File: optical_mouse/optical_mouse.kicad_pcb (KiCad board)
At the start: 2 copper layers, 44.5 x 45.7 mm, 18 parts, among them Q1 CSTLS_G, U1 ARDUINO_MINI

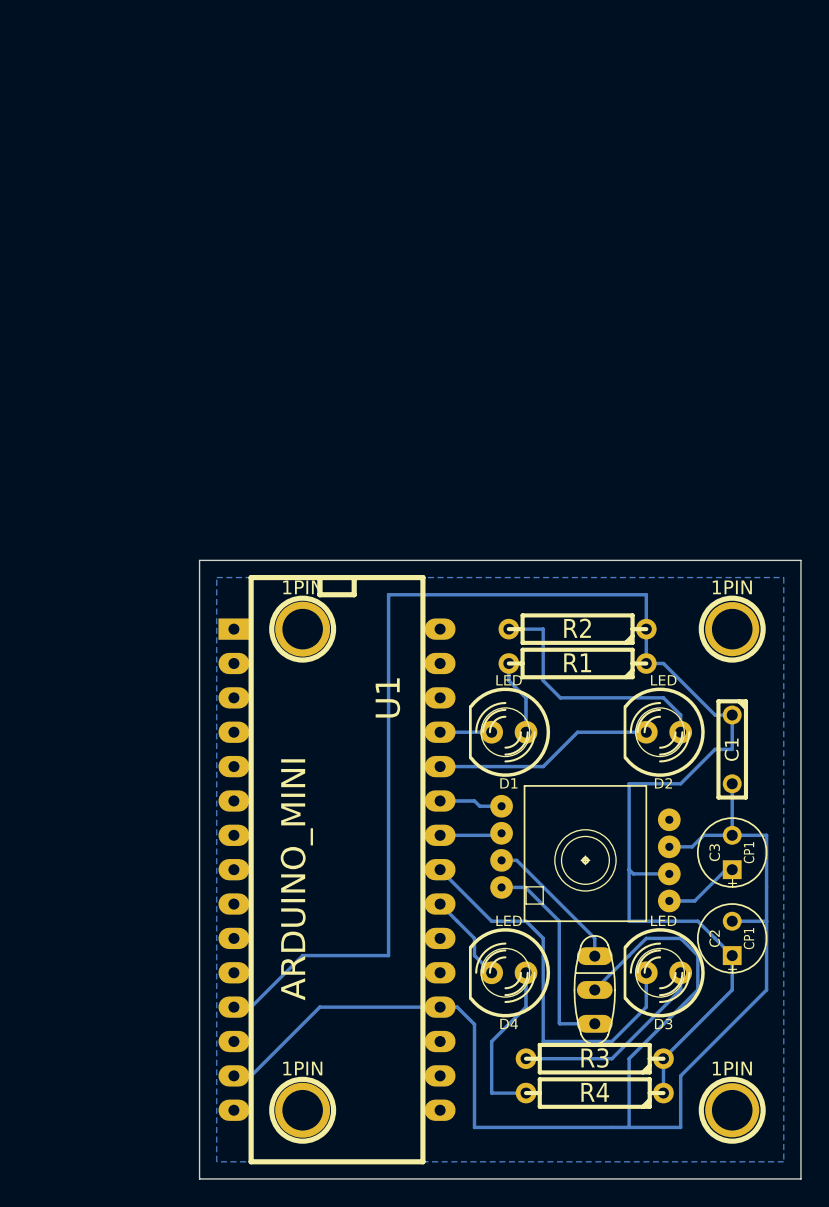
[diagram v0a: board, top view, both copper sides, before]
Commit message: re-layed out with correct mouse part
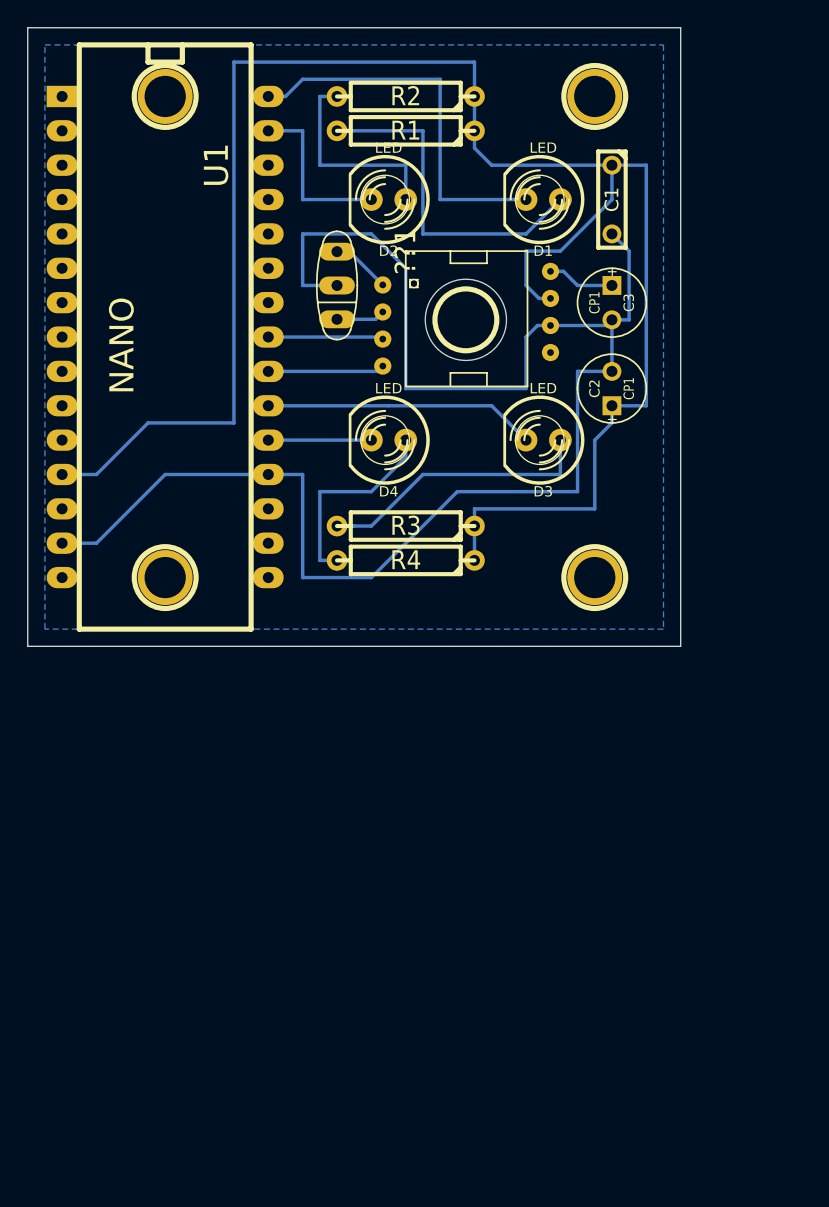
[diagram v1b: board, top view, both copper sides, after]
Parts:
- removed 1PIN (x4): P***, 1pin
- added ?: , 1pin, F.Cu at (154.9, 110.5)
- added ?: , 1pin, F.Cu at (186.7, 110.5)
- added ?: , 1pin, F.Cu at (186.7, 146.1)
- added ?: , 1pin, F.Cu at (154.9, 146.1)
- added ?: , 1pin, F.Cu at (177.2, 127.0)
- ??1: value ANDS-2610 -> (none); footprint adns-2610-DIP-8 -> adns-2610-DIP-8_(GORA)
- U1: value ARDUINO_MINI -> NANO
- moved Q1 55.4 mm to (167.6, 124.5), turned to 90 degrees
- moved ??1 52.6 mm to (172.7, 121.9), turned to 270 degrees
- moved D2 44.3 mm to (171.4, 118.1)
- moved R3 41.8 mm to (172.7, 142.2)
- moved R4 41.8 mm to (172.7, 144.8)
- moved C1 41.6 mm to (188.0, 118.1)
- moved C3 41.6 mm to (188.0, 125.7), turned to 270 degrees
- moved C2 41.6 mm to (188.0, 132.1)
- moved R2 41.4 mm to (172.7, 110.5)
- moved R1 41.4 mm to (172.7, 113.0)
- moved U1 41.4 mm to (154.9, 129.5)
- moved D3 40.4 mm to (182.9, 135.9)
- moved D4 40.4 mm to (171.4, 135.9)
- moved D1 39.5 mm to (182.9, 118.1)
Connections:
- ??1 pad 3: N-0000028 -> N-0000024
- ??1 pad 4: N-0000029 -> N-0000022
- D1 pad 2: N-000004 -> N-0000019
- D2 pad 2: N-000002 -> N-000006
- D3 pad 2: N-0000027 -> N-0000011
- D4 pad 2: N-0000025 -> N-0000018
- U1 pad 20: (no net) -> N-0000018
- U1 pad 21: (no net) -> N-0000011
- U1 pad 22: N-0000025 -> N-0000022
- U1 pad 23: N-0000027 -> N-0000024
- U1 pad 24: N-0000028 -> (no net)
- U1 pad 25: N-0000029 -> (no net)
- U1 pad 26: N-000002 -> (no net)
- U1 pad 27: N-000004 -> (no net)
- U1 pad 29: (no net) -> N-000006
- U1 pad 30: (no net) -> N-0000019
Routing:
- net N-0000027: track 28.6 -> 0.00 mm
- net N-0000019: track 0.00 -> 28.5 mm
- net N-0000011: track 0.00 -> 20.1 mm
- net N-000007: track 5.61 -> 25.2 mm
- net +5V: track 117.1 -> 134.7 mm
- net N-000002: track 16.3 -> 0.00 mm
- net N-000006: track 0.00 -> 12.7 mm
- net GND: track 105.9 -> 117.3 mm
- net N-0000032: track 15.5 -> 4.40 mm
- net N-0000022: track 0.00 -> 8.62 mm
- net N-0000024: track 0.00 -> 8.52 mm
- net N-0000018: track 0.00 -> 7.62 mm
- net N-0000031: track 10.6 -> 3.60 mm
- net N-0000025: track 6.66 -> 0.00 mm
- net N-000009: track 14.8 -> 20.6 mm
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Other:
- board size 44.5 x 45.7 mm -> 48.3 x 45.7 mm
- board text removed: "OptiMouseCam v 1.0 (C) Dave Berkeley 2015"

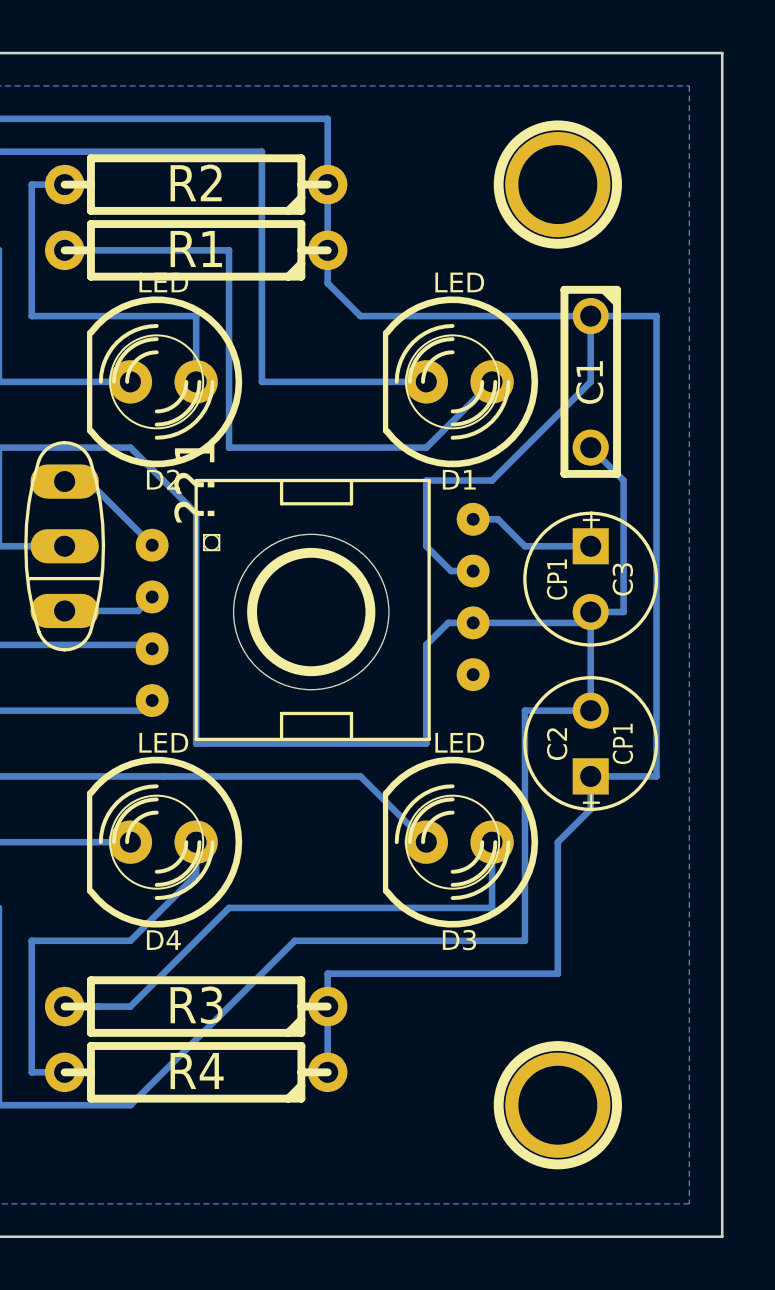
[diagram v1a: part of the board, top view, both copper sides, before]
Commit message: ensure camera hole is drilled in seedstudio
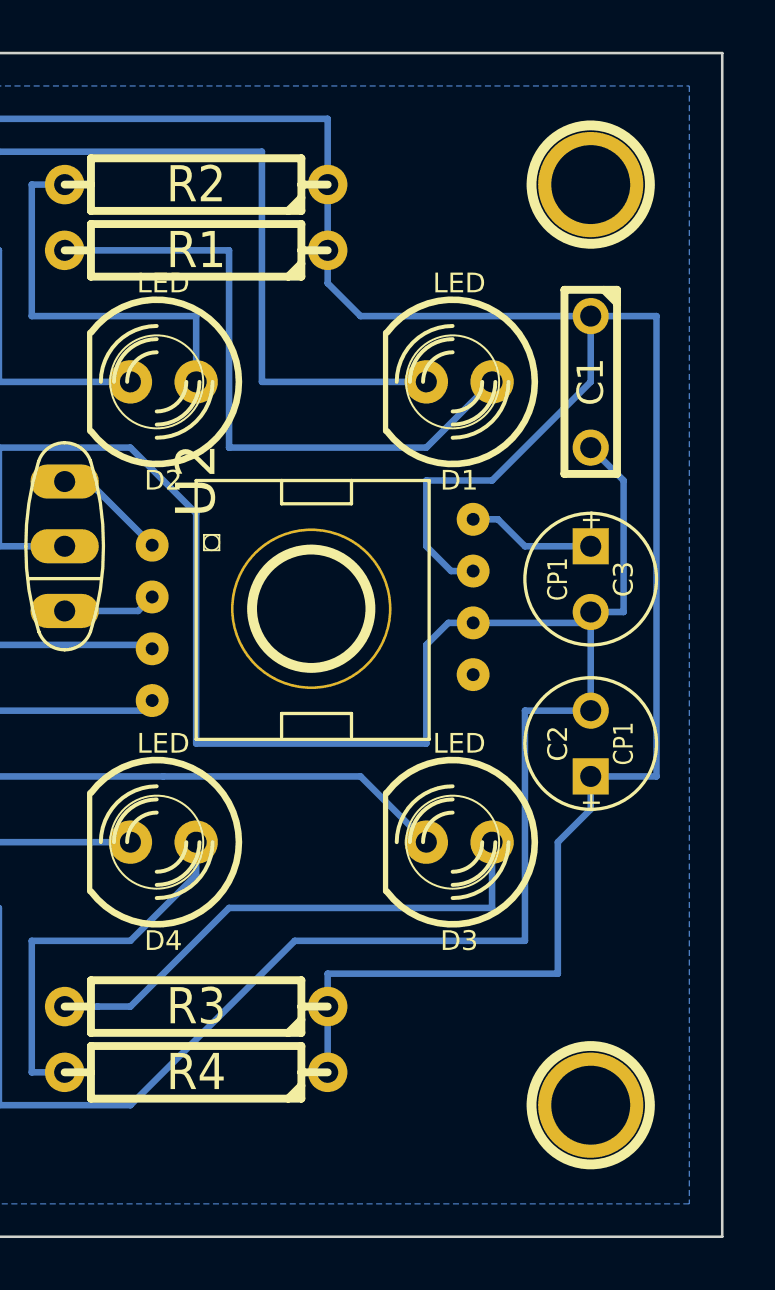
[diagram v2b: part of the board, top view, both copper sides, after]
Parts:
- moved ? 48.5 mm to (188.0, 146.1)
- moved ? 35.6 mm to (154.9, 110.5)
- moved ? 31.8 mm to (154.9, 146.1)
- moved ? 1.27 mm to (188.0, 110.5)
- moved ? 0.13 mm to (177.2, 126.9)
- renumbered ??1 to U2
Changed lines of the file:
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@@
     (mod_text_size 1 1)
     (mod_text_width 0.15)
-    (pad_size 6 6)
+    (pad_size 6.2 6.2)
     (pad_drill 6)
     (pad_to_mask_clearance 0)
@@
     (at 172.72 121.92 270)
     (attr virtual)
-    (fp_text reference ??1 (at 0 0 270) (layer F.SilkS)
+    (fp_text reference U2 (at 0 0 270) (layer F.SilkS)
       (effects (font (size 1.524 1.524) (thickness 0.15)))
     )
@@
   )
   (module 1pin (layer F.Cu)
-    (at 154.94 110.49)
+    (at 187.96 146.05)
     (descr "module 1 pin (ou trou mecanique de percage)")
     (tags DEV)
@@
     )
     (fp_circle (center 0 0) (end 0 -2.286) (layer F.SilkS) (width 0.381))
-    (pad "" np_thru_hole circle (at 0 0) (size 4.064 4.064) (drill 3.048)
+    (pad "" thru_hole circle (at 0 0) (size 4.064 4.064) (drill 3.048)
       (layers *.Cu *.Mask F.SilkS)
     )
   )
   (module 1pin (layer F.Cu)
-    (at 186.69 110.49)
+    (at 187.96 110.49)
     (descr "module 1 pin (ou trou mecanique de percage)")
     (tags DEV)
@@
     )
     (fp_circle (center 0 0) (end 0 -2.286) (layer F.SilkS) (width 0.381))
-    (pad "" np_thru_hole circle (at 0 0) (size 4.064 4.064) (drill 3.048)
-      (layers *.Cu *.Mask F.SilkS)
-    )
-  )
-  (module 1pin (layer F.Cu)
-    (at 186.69 146.05)
-    (descr "module 1 pin (ou trou mecanique de percage)")
-    (tags DEV)
-    (path 1pin)
-    (fp_text reference "" (at 0 -3.048) (layer F.SilkS)
-      (effects (font (size 1.016 1.016) (thickness 0.254)))
-    )
-    (fp_text value "" (at 0 2.794) (layer F.SilkS) hide
-      (effects (font (size 1.016 1.016) (thickness 0.254)))
-    )
-    (fp_circle (center 0 0) (end 0 -2.286) (layer F.SilkS) (width 0.381))
-    (pad "" np_thru_hole circle (at 0 0) (size 4.064 4.064) (drill 3.048)
+    (pad "" thru_hole circle (at 0 0) (size 4.064 4.064) (drill 3.048)
       (layers *.Cu *.Mask F.SilkS)
     )
@@
     )
     (fp_circle (center 0 0) (end 0 -2.286) (layer F.SilkS) (width 0.381))
-    (pad "" np_thru_hole circle (at 0 0) (size 4.064 4.064) (drill 3.048)
+    (pad "" thru_hole circle (at 0 0) (size 4.064 4.064) (drill 3.048)
       (layers *.Cu *.Mask F.SilkS)
     )
   )
   (module 1pin (layer F.Cu)
-    (at 177.165 127)
+    (at 154.94 110.49)
     (descr "module 1 pin (ou trou mecanique de percage)")
     (tags DEV)
@@
     )
     (fp_circle (center 0 0) (end 0 -2.286) (layer F.SilkS) (width 0.381))
-    (pad "" np_thru_hole circle (at 0 0) (size 6 6) (drill 6)
-      (layers *.Cu *.Mask F.SilkS)
-    )
+    (pad "" thru_hole circle (at 0 0) (size 4.064 4.064) (drill 3.048)
+      (layers *.Cu *.Mask F.SilkS)
+    )
+  )
+  (module 1pin (layer F.Cu)
+    (at 177.165 126.873)
+    (descr "module 1 pin (ou trou mecanique de percage)")
+    (tags DEV)
+    (path 1pin)
+    (fp_text reference "" (at 0 -3.048) (layer F.SilkS)
+      (effects (font (size 1.016 1.016) (thickness 0.254)))
+    )
+    (fp_text value "" (at 0 2.794) (layer F.SilkS) hide
+      (effects (font (size 1.016 1.016) (thickness 0.254)))
+    )
+    (fp_circle (center 0 0) (end 0 -2.286) (layer F.SilkS) (width 0.381))
+    (pad "" thru_hole circle (at 0 0) (size 6.2 6.2) (drill 6)
+      (layers *.Cu *.Mask F.SilkS)
+    )

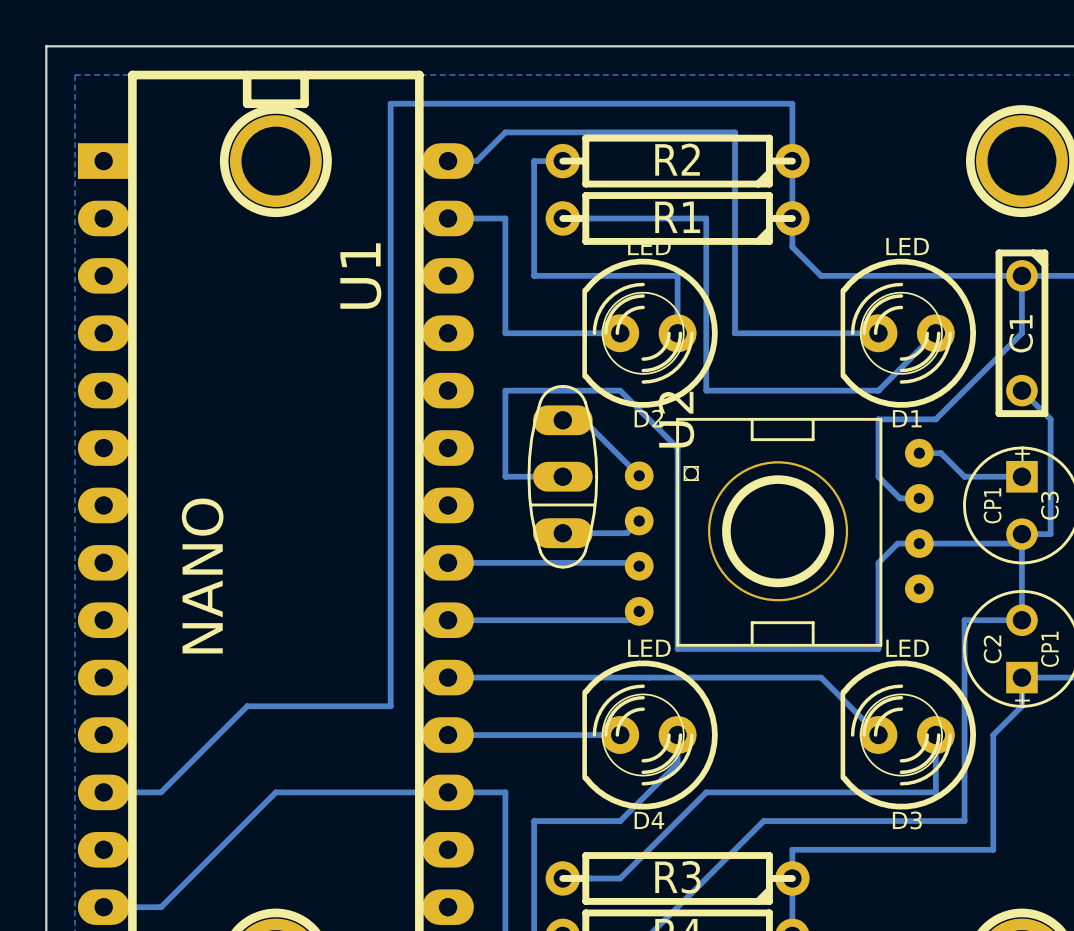
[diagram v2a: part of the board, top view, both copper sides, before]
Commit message: mirror copyright text
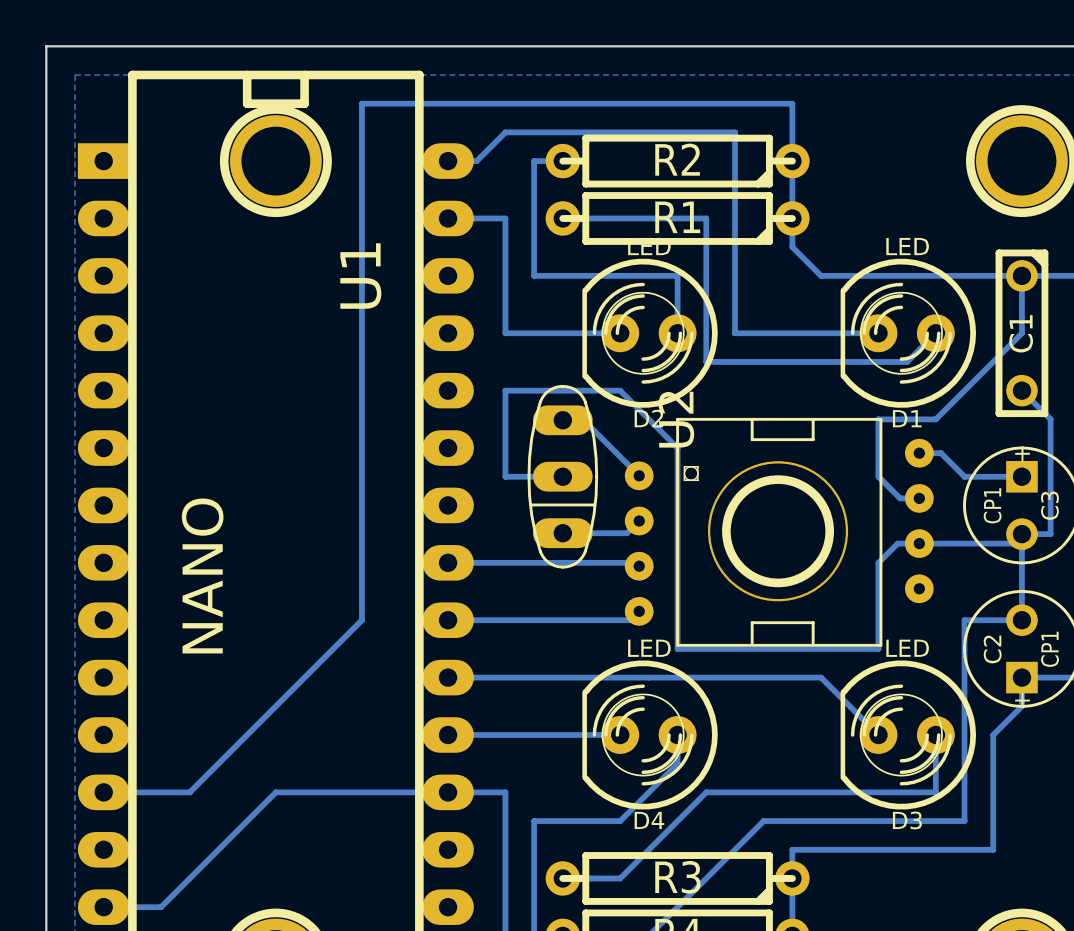
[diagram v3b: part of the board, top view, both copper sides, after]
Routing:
- net +5V: track 134.7 -> 132.5 mm
- net N-000007: track 25.2 -> 23.4 mm
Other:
- board text added: "OptMouseCam v1.0 (C) 2015 Dave Berkeley"
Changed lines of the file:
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@@
     (links 26)
     (no_connects 0)
-    (area 144.729999 105.359999 193.090001 151.180001)
+    (area 141.525713 105.359999 193.090001 151.180001)
     (thickness 1.6)
-    (drawings 4)
-    (tracks 91)
+    (drawings 5)
+    (tracks 90)
     (zones 0)
     (modules 19)
@@
     )
   )
+  (gr_text "OptMouseCam v1.0 (C) 2015 Dave Berkeley" (at 154.94 128.27 90) (layer B.SilkS)
+    (effects (font (size 0.8 0.8) (thickness 0.2)))
+  )
   (gr_line (start 144.78 151.13) (end 144.78 105.41) (angle 90) (layer Edge.Cuts) (width 0.1))
   (gr_line (start 193.04 151.13) (end 144.78 151.13) (angle 90) (layer Edge.Cuts) (width 0.1))
   (gr_line (start 193.04 105.41) (end 193.04 151.13) (angle 90) (layer Edge.Cuts) (width 0.1))
   (gr_line (start 144.78 105.41) (end 193.04 105.41) (angle 90) (layer Edge.Cuts) (width 0.1))
+  (segment (start 147.32 138.43) (end 151.13 138.43) (width 0.254) (layer B.Cu) (net 1))
+  (segment (start 177.8 107.95) (end 177.8 110.49) (width 0.254) (layer B.Cu) (net 1))
+  (segment (start 158.75 107.95) (end 177.8 107.95) (width 0.254) (layer B.Cu) (net 1))
+  (segment (start 158.75 130.81) (end 158.75 107.95) (width 0.254) (layer B.Cu) (net 1))
+  (segment (start 151.13 138.43) (end 158.75 130.81) (width 0.254) (layer B.Cu) (net 1))
   (segment (start 182.56758 125.41758) (end 183.41848 125.41758) (width 0.254) (layer B.Cu) (net 1))
   (segment (start 181.61 124.46) (end 182.56758 125.41758) (width 0.254) (layer B.Cu) (net 1))
@@
   (segment (start 186.69 140.97) (end 186.69 135.89) (width 0.254) (layer B.Cu) (net 1))
   (segment (start 177.8 140.97) (end 186.69 140.97) (width 0.254) (layer B.Cu) (net 1))
-  (segment (start 147.32 138.43) (end 149.86 138.43) (width 0.254) (layer B.Cu) (net 1))
-  (segment (start 177.8 107.95) (end 177.8 110.49) (width 0.254) (layer B.Cu) (net 1))
-  (segment (start 160.02 107.95) (end 177.8 107.95) (width 0.254) (layer B.Cu) (net 1))
-  (segment (start 160.02 134.62) (end 160.02 107.95) (width 0.254) (layer B.Cu) (net 1))
-  (segment (start 153.67 134.62) (end 160.02 134.62) (width 0.254) (layer B.Cu) (net 1))
-  (segment (start 149.86 138.43) (end 153.67 134.62) (width 0.254) (layer B.Cu) (net 1))
   (segment (start 177.8 113.03) (end 177.8 114.3) (width 0.254) (layer B.Cu) (net 1))
   (segment (start 177.8 114.3) (end 179.07 115.57) (width 0.254) (layer B.Cu) (net 1))
@@
   (segment (start 165.1 113.03) (end 165.1 118.11) (width 0.254) (layer B.Cu) (net 12))
   (segment (start 167.64 113.03) (end 173.99 113.03) (width 0.254) (layer B.Cu) (net 13))
-  (segment (start 181.61 120.65) (end 184.15 118.11) (width 0.254) (layer B.Cu) (net 13))
-  (segment (start 173.99 120.65) (end 181.61 120.65) (width 0.254) (layer B.Cu) (net 13))
-  (segment (start 173.99 113.03) (end 173.99 120.65) (width 0.254) (layer B.Cu) (net 13))
+  (segment (start 182.88 119.38) (end 184.15 118.11) (width 0.254) (layer B.Cu) (net 13))
+  (segment (start 173.99 119.38) (end 182.88 119.38) (width 0.254) (layer B.Cu) (net 13))
+  (segment (start 173.99 113.03) (end 173.99 119.38) (width 0.254) (layer B.Cu) (net 13))
   (segment (start 167.64 110.49) (end 166.37 110.49) (width 0.254) (layer B.Cu) (net 14))
   (segment (start 172.72 115.57) (end 172.72 118.11) (width 0.254) (layer B.Cu) (net 14))
